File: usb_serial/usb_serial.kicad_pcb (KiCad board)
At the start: 2 copper layers, 18 x 30 mm, 13 parts, among them J2 USB_B_Micro, J3 Conn_01x04_Pin, U1 FT232RL

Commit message: Silk screen realigned
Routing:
- net GND: track 11.9 -> 11.3 mm
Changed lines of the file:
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@@
 		(tags "USB Micro B horizontal SMD")
 		(property "Reference" "J2"
-			(at 0 -3.5 0)
+			(at 5.01 -1.06 0)
 			(layer "F.SilkS")
 			(effects
@@
 		(tags "capacitor")
 		(property "Reference" "C4"
-			(at -0.04 -1.3 -90)
+			(at 0.5 -1.56 0)
 			(layer "F.SilkS")
 			(effects
@@
 		(tags "capacitor")
 		(property "Reference" "C1"
-			(at 0 -1.43 0)
+			(at 0.09 1.55 0)
 			(layer "F.SilkS")
 			(effects
@@
 	)
 	(segment
-		(start 145.94 75.64)
-		(end 146.82 75.64)
+		(start 146.82 75.64)
+		(end 145.94 75.64)
 		(width 0.4)
 		(layer "F.Cu")
@@
 	)
 	(segment
-		(start 144.265 67.855)
-		(end 144.43 68.02)
-		(width 0.4)
-		(layer "F.Cu")
-		(net 18)
-	)
-	(segment
-		(start 146.82 75.64)
-		(end 146.84 75.66)
+		(start 144.28 65.79)
+		(end 144.28 66.635)
 		(width 0.4)
 		(layer "F.Cu")
@@
 	)
 	(segment
-		(start 142.7 74.825)
-		(end 141.395 74.825)
+		(start 144.28 66.635)
+		(end 144.265 66.65)
 		(width 0.4)
 		(layer "F.Cu")
@@
 	)
 	(segment
-		(start 144.265 66.65)
-		(end 144.265 67.855)
+		(start 142.7 74.825)
+		(end 141.395 74.825)
 		(width 0.4)
 		(layer "F.Cu")
@@
 	)
 	(via
-		(at 144.43 68.02)
+		(at 144.28 65.79)
 		(size 0.5)
 		(drill 0.3)
@@
 	)
 	(via
-		(at 146.84 75.66)
+		(at 146.82 75.64)
 		(size 0.5)
 		(drill 0.3)

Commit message: Mechanical Diagram added
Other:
- board text added: "Unit: mm"
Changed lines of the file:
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@@
 			(at 0 5.2 0)
 			(layer "F.Fab")
+			(hide yes)
 			(effects
 				(font
@@
 			(at 0 1.16 0)
 			(layer "F.Fab")
+			(hide yes)
 			(effects
 				(font
@@
 			(at 0 1.65 90)
 			(layer "F.Fab")
+			(hide yes)
 			(effects
 				(font
@@
 			(at 0 1.16 90)
 			(layer "F.Fab")
+			(hide yes)
 			(effects
 				(font
@@
 			(at 0 1.65 90)
 			(layer "F.Fab")
+			(hide yes)
 			(effects
 				(font
@@
 			(at 0 1.68 90)
 			(layer "F.Fab")
+			(hide yes)
 			(effects
 				(font
@@
 			(at 0 1.17 0)
 			(layer "F.Fab")
+			(hide yes)
 			(effects
 				(font
@@
 			(at 0 1.17 0)
 			(layer "F.Fab")
+			(hide yes)
 			(effects
 				(font
@@
 			(at 0 1.65 90)
 			(layer "F.Fab")
+			(hide yes)
 			(effects
 				(font
@@
 			(at 0 1.17 0)
 			(layer "F.Fab")
+			(hide yes)
 			(effects
 				(font
@@
 			(at 0 9.95 90)
 			(layer "F.Fab")
+			(hide yes)
 			(effects
 				(font
@@
 			(at 0 1.43 0)
 			(layer "F.Fab")
+			(hide yes)
 			(effects
 				(font
@@
 		)
 	)
+	(gr_text "Unit: mm"
+		(at 155.98 98.12 0)
+		(layer "F.Fab")
+		(effects
+			(font
+				(size 2 2)
+				(thickness 0.4)
+				(bold yes)
+			)
+			(justify left bottom)
+		)
+	)
+	(dimension
+		(type aligned)
+		(layer "F.Fab")
+		(pts
+			(xy 130 90) (xy 130 60)
+		)
+		(height -2.83)
+		(gr_text "30.00"
+			(at 126.02 75 90)
+			(layer "F.Fab")
+			(effects
+				(font
+					(size 1 1)
+					(thickness 0.15)
+				)
+			)
+		)
+		(format
+			(prefix "")
+			(suffix "")
+			(units 3)
+			(units_format 0)
+			(precision 2)
+		)
+		(style
+			(thickness 0.1)
+			(arrow_length 1.27)
+			(text_position_mode 0)
+			(extension_height 0.58642)
+			(extension_offset 0.5) keep_text_aligned)
+	)
+	(dimension
+		(type aligned)
+		(layer "F.Fab")
+		(pts
+			(xy 135.35 61.84) (xy 130 61.84)
+		)
+		(height 5.42)
+		(gr_text "5.35"
+			(at 132.675 55.27 0)
+			(layer "F.Fab")
+			(effects
+				(font
+					(size 1 1)
+					(thickness 0.15)
+				)
+			)
+		)
+		(format
+			(prefix "")
+			(suffix "")
+			(units 3)
+			(units_format 0)
+			(precision 2)
+		)
+		(style
+			(thickness 0.1)
+			(arrow_length 1.27)
+			(text_position_mode 0)
+			(extension_height 0.58642)
+			(extension_offset 0.5) keep_text_aligned)
+	)
+	(dimension
+		(type aligned)
+		(layer "F.Fab")
+		(pts
+			(xy 138.99 87.4) (xy 130 87.4)
+		)
+		(height -7.35)
+		(gr_text "8.99"
+			(at 141.25 94.81 0)
+			(layer "F.Fab")
+			(effects
+				(font
+					(size 1 1)
+					(thickness 0.15)
+				)
+			)
+		)
+		(format
+			(prefix "")
+			(suffix "")
+			(units 3)
+			(units_format 0)
+			(precision 2)
+		)
+		(style
+			(thickness 0.1)
+			(arrow_length 1.27)
+			(text_position_mode 2)
+			(extension_height 0.58642)
+			(extension_offset 0.5) keep_text_aligned)
+	)
+	(dimension
+		(type aligned)
+		(layer "F.Fab")
+		(pts
+			(xy 133.92 88.035) (xy 130 88.035)
+		)
+		(height -4.545)
+		(gr_text "3.92"
+			(at 136.31 92.57 0)
+			(layer "F.Fab")
+			(effects
+				(font
+					(size 1 1)
+					(thickness 0.15)
+				)
+			)
+		)
+		(format
+			(prefix "")
+			(suffix "")
+			(units 3)
+			(units_format 0)
+			(precision 2)
+		)
+		(style
+			(thickness 0.1)
+			(arrow_length 1.27)
+			(text_position_mode 2)
+			(extension_height 0.58642)
+			(extension_offset 0.5) keep_text_aligned)
+	)
+	(dimension
+		(type aligned)
+		(layer "F.Fab")
+		(pts
+			(xy 142.65 61.34) (xy 130 61.34)
+		)
+		(height 8.78)
+		(gr_text "12.65"
+			(at 136.325 51.41 0)
+			(layer "F.Fab")
+			(effects
+				(font
+					(size 1 1)
+					(thickness 0.15)
+				)
+			)
+		)
+		(format
+			(prefix "")
+			(suffix "")
+			(units 3)
+			(units_format 0)
+			(precision 2)
+		)
+		(style
+			(thickness 0.1)
+			(arrow_length 1.27)
+			(text_position_mode 0)
+			(extension_height 0.58642)
+			(extension_offset 0.5) keep_text_aligned)
+	)
+	(dimension
+		(type aligned)
+		(layer "F.Fab")
+		(pts
+			(xy 130 90) (xy 148 90)
+		)
+		(height 8.45)
+		(gr_text "18.00"
+			(at 139 97.3 0)
+			(layer "F.Fab")
+			(effects
+				(font
+					(size 1 1)
+					(thickness 0.15)
+				)
+			)
+		)
+		(format
+			(prefix "")
+			(suffix "")
+			(units 3)
+			(units_format 0)
+			(precision 2)
+		)
+		(style
+			(thickness 0.1)
+			(arrow_length 1.27)
+			(text_position_mode 0)
+			(extension_height 0.58642)
+			(extension_offset 0.5) keep_text_aligned)
+	)
 	(segment

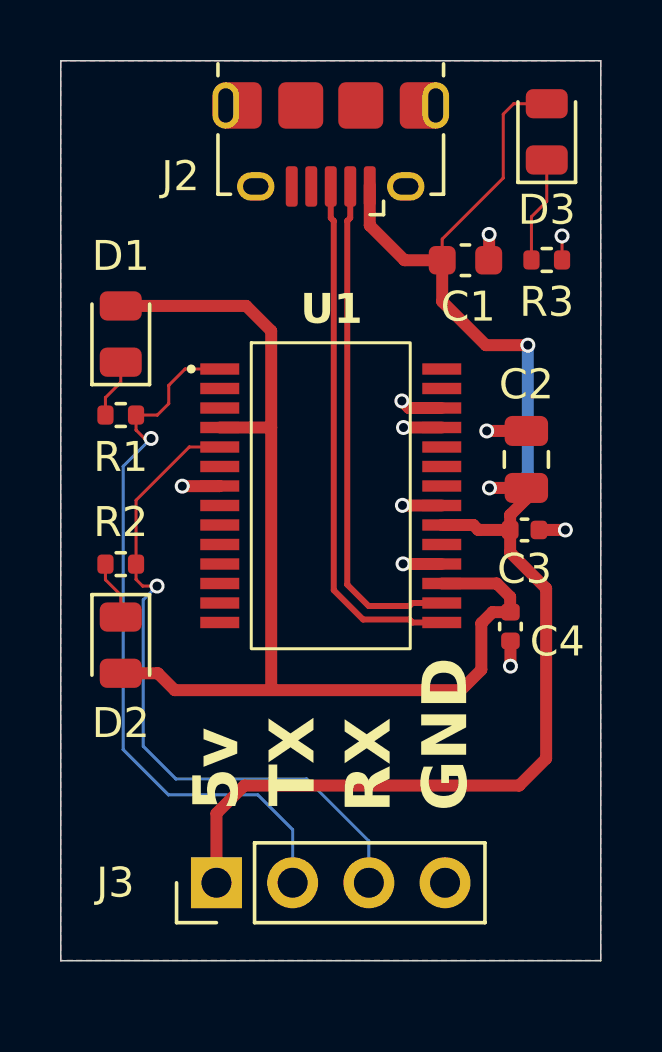
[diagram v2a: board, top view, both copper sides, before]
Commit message: [FIX] Changed 4pin 2.54mm header from vertical one to a right-angled one
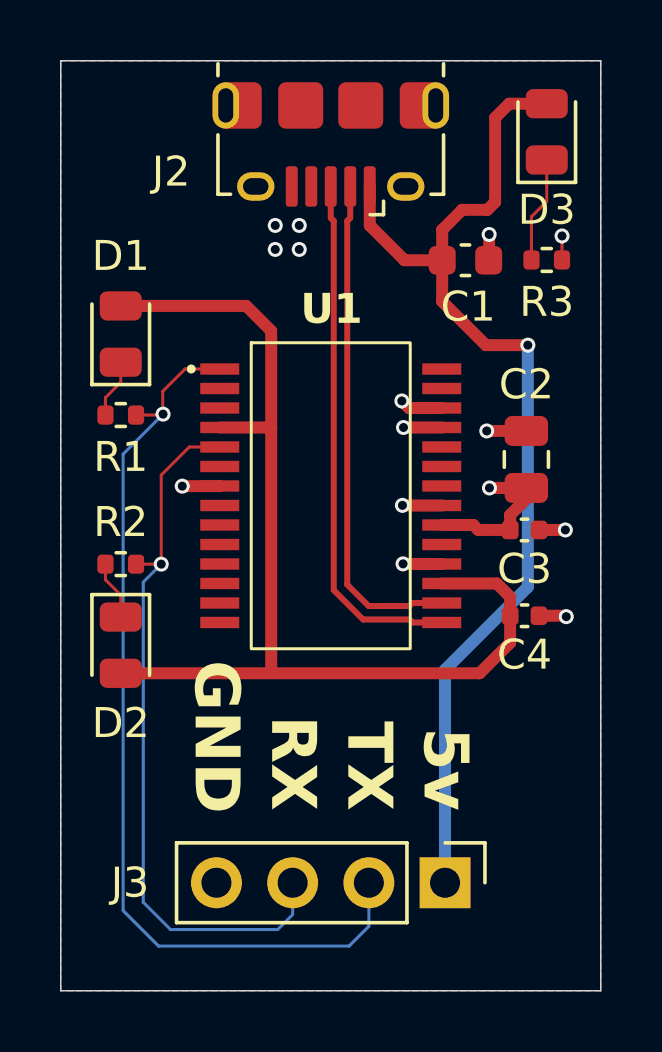
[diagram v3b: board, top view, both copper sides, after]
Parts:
- moved J3 7.62 mm to (142.8, 87.4), turned to -90 degrees
- moved C4 0.59 mm to (145.5, 78.5), turned to 0 degrees
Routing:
- net /UART_TX: track 24.2 -> 31.4 mm
- net +5V: track 49.5 -> 42.5 mm
- net /UART_RX: track 22.7 -> 24.3 mm
- net +3.3V: track 37.2 -> 35.9 mm
- net GND: vias 10 -> 14
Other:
- board size 18 x 30 mm -> 18 x 31 mm
